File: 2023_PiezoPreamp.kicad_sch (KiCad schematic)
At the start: 0 parts

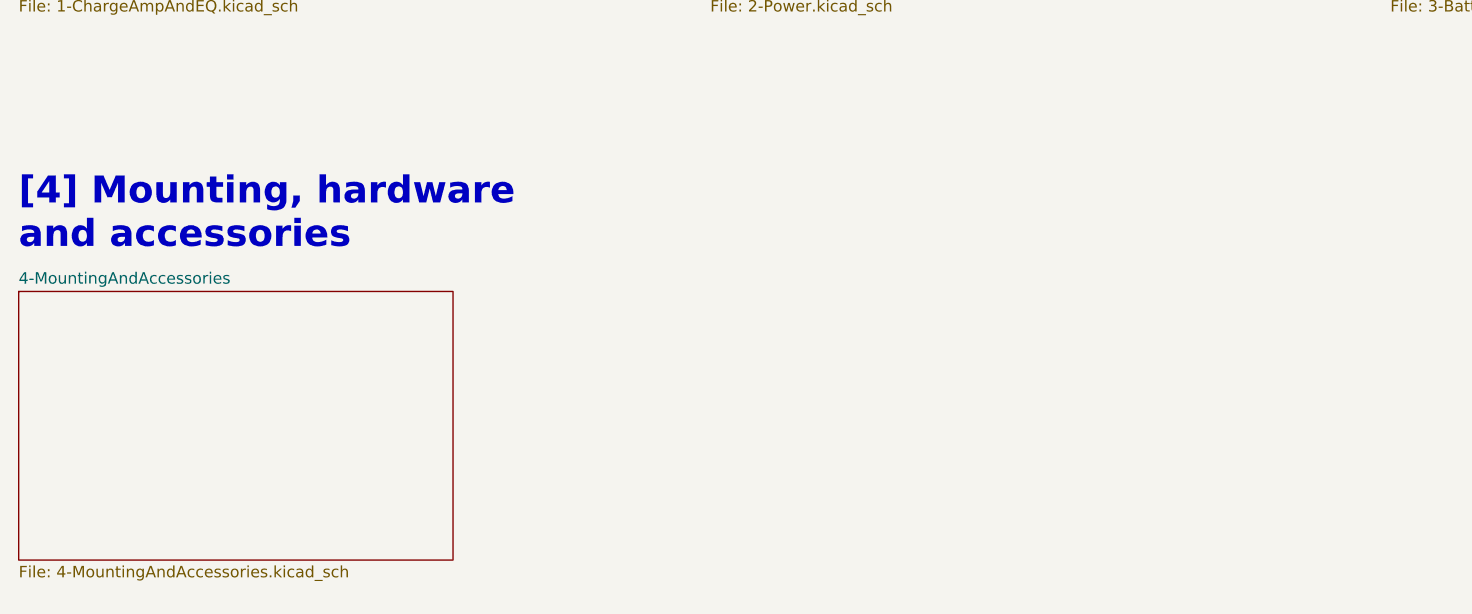
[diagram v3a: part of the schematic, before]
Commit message: improving the schematic - v3.0. Very crude draft of board layout with battery holder underneath the PCB
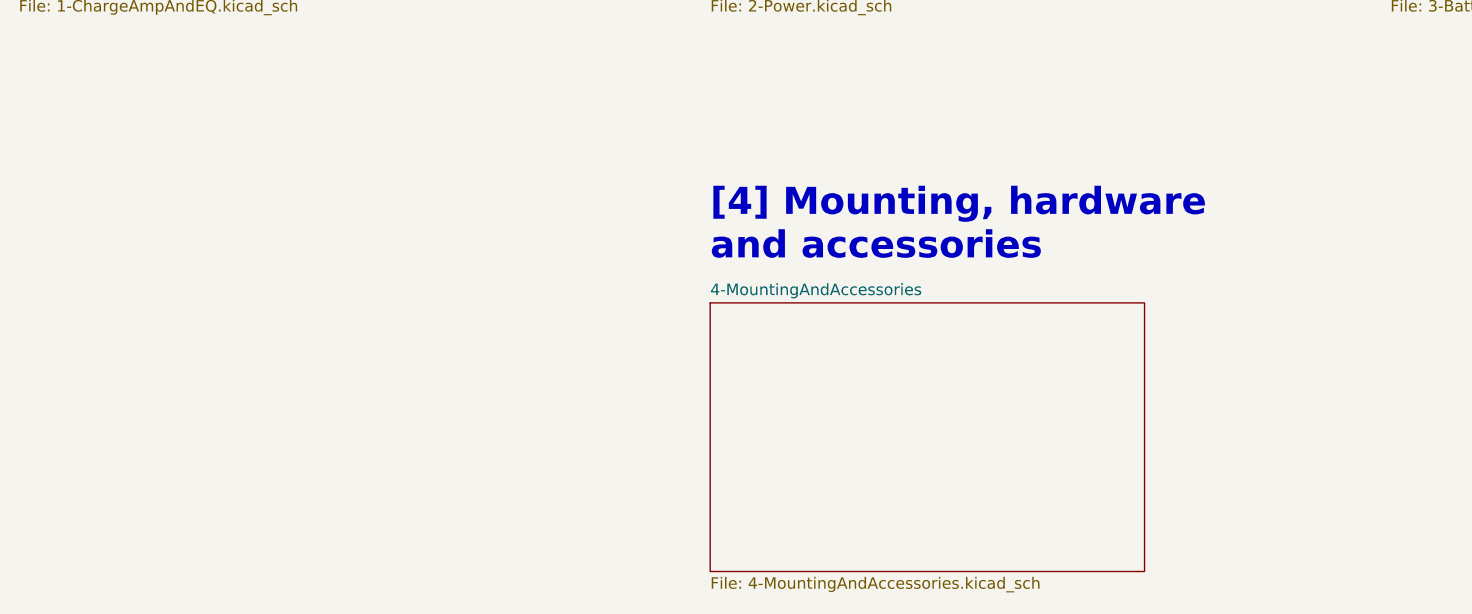
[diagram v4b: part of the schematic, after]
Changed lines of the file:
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@@
   (title_block
     (title "Piezo Preamp + EQ")
-    (date "2024-01-17")
-    (rev "2.3")
+    (date "2024-02-08")
+    (rev "3.0")
     (company "Arx")
-    (comment 1 "v2.1: PCB: fixing pad sizes - some were too small")
-    (comment 2 "v2.2: scheme, PCB: fixing T and R pins on audio jacks - they were swapped before")
-    (comment 3 "v2.3: PCB: adjusting board size to better fit the enclosure. Increasing opamp pad sizes.")
+    (comment 1 "v3.0: +ON/OFF sw w/ true bypass, +BI mode sw, + DC jack, external pots, -LED trimpot")
   )
-  (text "[4] Mounting, hardware\nand accessories" (at 42.545 124.46 0)
+  (text "[4] Mounting, hardware\nand accessories" (at 119.38 125.73 0)
     (effects (font (size 3 3) (thickness 1) bold) (justify left bottom))
   )
@@
     )
   )
-  (sheet (at 42.545 128.905) (size 48.26 29.845) (fields_autoplaced)
+  (sheet (at 119.38 130.175) (size 48.26 29.845) (fields_autoplaced)
     (stroke (width 0.1524) (type solid))
     (fill (color 0 0 0 0.0000))
-    (property "Sheetname" "4-MountingAndAccessories" (at 42.545 128.1934 0)
+    (property "Sheetname" "4-MountingAndAccessories" (at 119.38 129.4634 0)
       (effects (font (size 1.27 1.27)) (justify left bottom))
     )
-    (property "Sheetfile" "4-MountingAndAccessories.kicad_sch" (at 42.545 159.3346 0)
+    (property "Sheetfile" "4-MountingAndAccessories.kicad_sch" (at 119.38 160.6046 0)
       (effects (font (size 1.27 1.27)) (justify left top))
     )

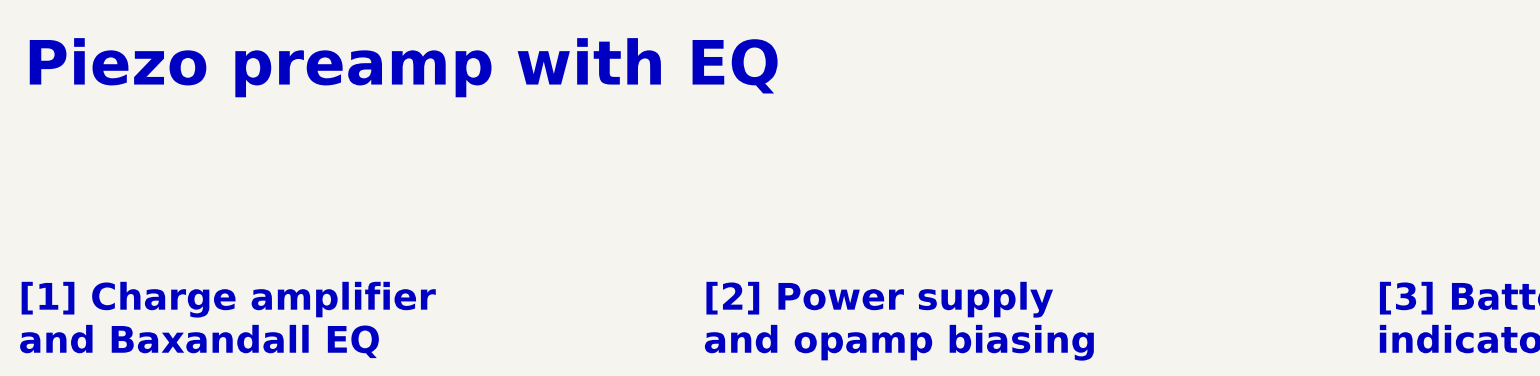
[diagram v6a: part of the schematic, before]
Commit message: Schematic: replacing SP3T HPF switch with SP4T again, adding the new HPF cutoff position, moving libraries around. Choosing different 150R resistor because of availability
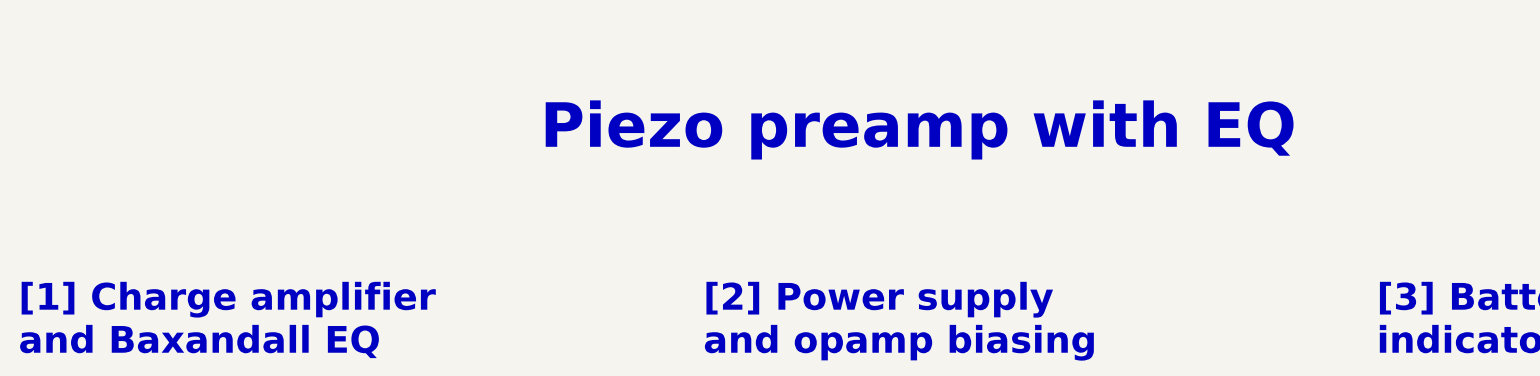
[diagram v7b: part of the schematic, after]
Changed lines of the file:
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@@
 	(title_block
 		(title "Piezo Preamp + EQ")
-		(date "2024-02-15")
+		(date "2024-02-20")
 		(rev "3.0")
 		(company "Arx")
-		(comment 1 "v3.0: +ON/OFF sw w/ true bypass, +BI mode sw, + DC jack, external pots, -LED trimpot")
+		(comment 1 "changing switches, reducing BOM")
+		(comment 2 "v3.0: +ON/OFF sw w/ true bypass, +BI mode sw, + DC jack, external pots, -LED trimpot,")
 	)
 	(text "[4] Mounting, hardware\nand accessories"
@@
 	(text "Piezo preamp with EQ"
 		(exclude_from_sim no)
-		(at 43.18 31.115 0)
+		(at 143.51 38.1 0)
 		(effects
 			(font
@@
 				(bold yes)
 			)
-			(justify left bottom)
+			(justify bottom)
 		)
 	)
